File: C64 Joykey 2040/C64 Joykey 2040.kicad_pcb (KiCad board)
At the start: 2 copper layers, 99.7 x 74.9 mm, 62 parts, among them J1 Port_1, J2 Port_2, M1 Mounting, M2 Mounting, M3 Mounting, M4 Mounting, Q1 2N3904, SW1 P2_FIRE1, SW10 P1_FIRE2, SW11 P1_FIRE3, SW12 P1_FIRE4, SW2 P2_FIRE2, SW3 P2_FIRE3, SW4 UP, SW5 DOWN, SW6 LEFT, SW7 RIGHT, SW8 RESET, SW9 P1_FIRE1

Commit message: First layout drafted
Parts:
- removed A1: Arduino_Pro_Micro, arduino_pro_micro:Arduino_Pro_Micro
- removed JP4: DEFAULT_FW, solder_bridge:bridge
- removed JP5: LED_SEL, solder_bridge:select
- removed JP6: DEFAULT_FW, solder_bridge:bridge_r
- removed JP9: ARD_EN, Connector_PinHeader_2.54mm:PinHeader_1x02_P2.54mm_Vertical
- removed R14, R15, R16, R17, R18, R19, R20, R21, R5: 10k, Resistor_THT:R_Axial_DIN0207_L6.3mm_D2.5mm_P10.16mm_Horizontal
- added D12: 1N4148, Diode_THT:D_DO-35_SOD27_P7.62mm_Horizontal, F.Cu at (151.1, 109.9)
- added D13: 1N4148, Diode_THT:D_DO-35_SOD27_P7.62mm_Horizontal, F.Cu at (169.5, 117.5)
- added D14: 1N4148, Diode_THT:D_DO-35_SOD27_P7.62mm_Horizontal, F.Cu at (172.7, 117.5)
- added D15: 1N4148, Diode_THT:D_DO-35_SOD27_P7.62mm_Horizontal, F.Cu at (179.1, 117.5)
- added D16: 1N4148, Diode_THT:D_DO-35_SOD27_P7.62mm_Horizontal, F.Cu at (205.1, 106.0)
- added D17: 1N4148, Diode_THT:D_DO-35_SOD27_P7.62mm_Horizontal, F.Cu at (175.9, 117.5)
- added D18: 1N4148, Diode_THT:D_DO-35_SOD27_P7.62mm_Horizontal, F.Cu at (182.2, 117.5)
- added D19: 1N4148, Diode_THT:D_DO-35_SOD27_P7.62mm_Horizontal, F.Cu at (194.3, 111.8)
- added D20: 1N4148, Diode_THT:D_DO-35_SOD27_P7.62mm_Horizontal, F.Cu at (190.5, 102.2)
- added D21: 1N4148, Diode_THT:D_DO-35_SOD27_P7.62mm_Horizontal, F.Cu at (205.1, 96.5)
- added D22: 1N4148, Diode_THT:D_DO-35_SOD27_P7.62mm_Horizontal, F.Cu at (205.1, 99.7)
- added D23: 1N4148, Diode_THT:D_DO-35_SOD27_P7.62mm_Horizontal, F.Cu at (205.1, 102.9)
- added D24: 1N4148, Diode_THT:D_DO-35_SOD27_P7.62mm_Horizontal, F.Cu at (143.5, 111.8)
- added D25: 1N4148, Diode_THT:D_DO-35_SOD27_P7.62mm_Horizontal, F.Cu at (185.4, 117.5)
- added J3: LED_EN, TestPoint:TestPoint_THTPad_D1.5mm_Drill0.7mm, F.Cu at (217.8, 122.6)
- added J4: Expansion, Connector_PinHeader_2.54mm:PinHeader_1x04_P2.54mm_Vertical, F.Cu at (144.1, 133.3)
- added R23: 10k, Resistor_THT:R_Axial_DIN0207_L6.3mm_D2.5mm_P10.16mm_Horizontal, F.Cu at (217.8, 116.8)
- added SW13: P1_FIRE6, Button_Switch_THT:SW_Tactile_SPST_Angled_PTS645Vx31-2LFS, F.Cu at (206.7, 154.7)
- added U1: RP2040-Zero, pi_pico:RP2040-Zero, F.Cu at (177.2, 108.6)
- D2: value SYS -> POL
- D4: value 1n4148 -> 1N4148
- Q1: footprint 2n3904:2N3904_TO-92_Horizontal_FlatSideDown -> Package_TO_SOT_THT:TO-92_Inline_Wide
- R4: value 330 -> 100
- SW1: value P2_FIRE1 -> UP
- SW11: value P1_FIRE3 -> P2_FIRE3; footprint Button_Switch_THT:SW_Tactile_SPST_Angled_PTS645Vx31-2LFS -> Button_Switch_Keyboard:SW_Cherry_MX_1.00u_PCB
- SW12: value P1_FIRE4 -> P1_FIRE5
- SW2: value P2_FIRE2 -> DOWN
- SW3: value P2_FIRE3 -> LEFT
- SW4: value UP -> RIGHT
- SW5: value DOWN -> P1_FIRE4; footprint Button_Switch_Keyboard:SW_Cherry_MX_1.00u_PCB -> Button_Switch_THT:SW_Tactile_SPST_Angled_PTS645Vx31-2LFS
- SW6: value LEFT -> P2_FIRE1
- SW7: value RIGHT -> P1_FIRE1; footprint Button_Switch_Keyboard:SW_Cherry_MX_1.00u_PCB -> Button_Switch_THT:SW_Tactile_SPST_Angled_PTS645Vx31-2LFS
- SW8: value RESET -> P1_FIRE3; footprint Button_Switch_THT:SW_PUSH_6mm -> Button_Switch_THT:SW_Tactile_SPST_Angled_PTS645Vx31-2LFS
- SW9: value P1_FIRE1 -> P2_FIRE2; footprint Button_Switch_THT:SW_Tactile_SPST_Angled_PTS645Vx31-2LFS -> Button_Switch_Keyboard:SW_Cherry_MX_1.00u_PCB
- moved SW7 67.4 mm to (155.4, 154.7)
- moved SW11 56.5 mm to (154.3, 104.1)
- moved SW1 51.5 mm to (201.3, 125.1)
- moved SW2 51.5 mm to (201.3, 146.1)
- moved SW3 49.3 mm to (180.3, 146.1)
- moved G*** 48.7 mm to (177.5, 124.0)
- moved D4 34.1 mm to (147.3, 104.1), turned to -90 degrees
- moved R13 32.1 mm to (228.0, 127.6)
- moved SW8 31.6 mm to (179.4, 154.7), turned to 180 degrees
- moved SW5 30.7 mm to (230.7, 154.7)
- moved SW4 29.6 mm to (222.2, 146.1)
- moved SW9 29.6 mm to (154.3, 125.1)
- moved R1 28.4 mm to (217.8, 113.0)
- moved SW6 26.0 mm to (154.3, 146.1)
- moved R2 25.9 mm to (217.8, 109.2)
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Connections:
- D4 pad 1: /FIRE1_OUT -> Net-(D12-K)
- D4 pad 2: Net-(D4-A) -> FIRE3_POL
- R13 pad 2: /UNDERGLOW -> Net-(J3-Pin_1)
- R3 pad 2: Net-(JP5-C) -> VCC
- R4 pad 2: /SYS -> Net-(D12-K)
- SW1 pad 1: Net-(JP4-Pad1) -> P2_UP
- SW10 pad 2: FIRE2_POL -> GND
- SW11 pad 1: P1_FIRE3 -> Net-(JP3-C)
- SW12 pad 1: P1_FIRE4 -> P1_FIRE5
- SW2 pad 1: Net-(JP6-Pad1) -> P2_DOWN
- SW2 pad 2: FIRE2_POL -> GND
- SW3 pad 1: Net-(JP3-C) -> P2_LEFT
- SW3 pad 2: FIRE3_POL -> GND
- SW4 pad 1: P2_UP -> P2_RIGHT
- SW5 pad 1: P2_DOWN -> P1_FIRE4
- SW6 pad 1: P2_LEFT -> P2_FIRE1
- SW7 pad 1: P2_RIGHT -> P1_FIRE1
- SW8 pad 1: Net-(A1-RST) -> P1_FIRE3
- SW9 pad 1: P1_FIRE1 -> P2_FIRE2
- SW9 pad 2: GND -> FIRE2_POL
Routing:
- net Net-(A1-D18): track 78.1 -> 0.00 mm
- net P1_FIRE5: track 0.00 -> 78.0 mm, vias 0 -> 3
- net P1_FIRE2: track 174.7 -> 100.8 mm, vias 2 -> 3
- net I2C_SDA: track 0.00 -> 73.6 mm
- net I2C_SCL: track 0.00 -> 68.3 mm
- net +3V3: track 0.00 -> 65.1 mm
- net /B2: track 0.00 -> 62.9 mm, vias 0 -> 2
- net P1_FIRE6: track 0.00 -> 51.7 mm, vias 0 -> 2
- net /FIRE1_IN: track 51.5 -> 0.00 mm, vias 2 -> 0
- net Net-(A1-D14): track 51.1 -> 0.00 mm, vias 2 -> 0
- net FIRE3_POL: track 142.6 -> 91.7 mm, vias 4 -> 2
- net Net-(A1-RST): track 49.2 -> 0.00 mm, vias 2 -> 0
- net /SYS: track 49.2 -> 0.00 mm, vias 1 -> 0
- net Net-(JP4-Pad1): track 48.3 -> 0.00 mm
- net Net-(A1-D19): track 46.0 -> 0.00 mm, vias 2 -> 0
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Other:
- board text added: "(A1)"
- board text added: "(B1)"
- board text added: "(B2)"
- board text added: "(B3)"
- board text added: "(B4)"
- board text added: "(R1)"
- board text added: "(R2)"
- board text added: "(S1)"
- board text added: "(S2)"
- board text added: "2040 Revision A github.com/tebl"
- board text added: "IMPORTANT! Always configure FIRE2/FIRE3 polarity according to what's required by the system. Leave unjumpered (N/C) if you are not sure. You break it, you fix it!"
- board text added: "P1 F5"
- board text added: "P1 F6"
- board text removed: "1-2 Always ON 2-3 Arduino"
- board text removed: "ARD_EN"
- board text removed: "Default FW"
- board text removed: "IMPORTANT! Configure FIRE2/FIRE3 polarity according to what is required by the system, leave unjumpered (N/C) if you are not sure. You break it, you fix it!"
- board text removed: "Install Arduino Pro Micro, if needed for USB function. Hold down LEFT + RIGHT key on powerup to enable. FIRE2/3 polarity must be set to GND, keys will be disabled in USB-mode if not."
- board text removed: "PCB Revision F github.com/tebl"

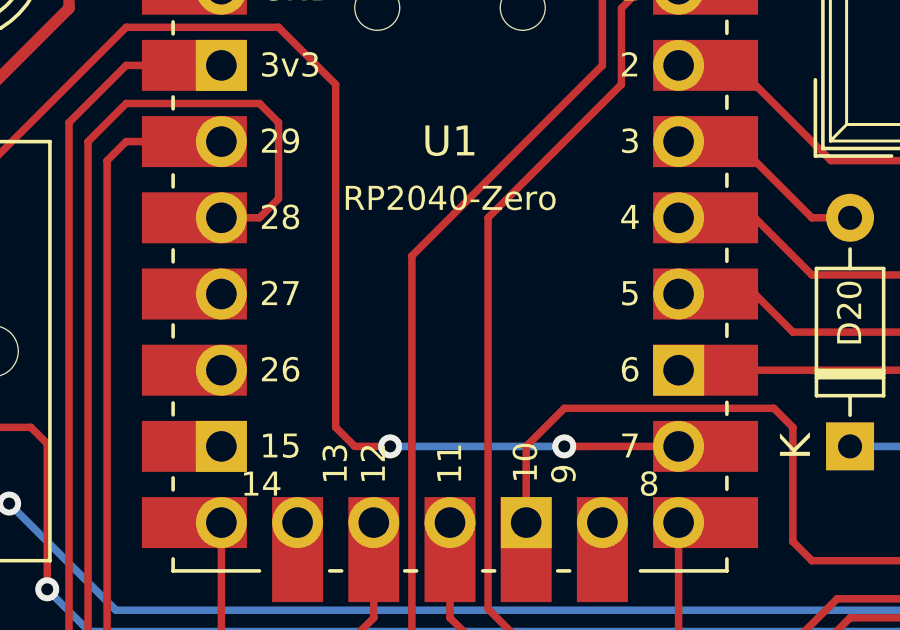
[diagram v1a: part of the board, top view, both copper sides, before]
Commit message: Arcade 2040, and some cleanup
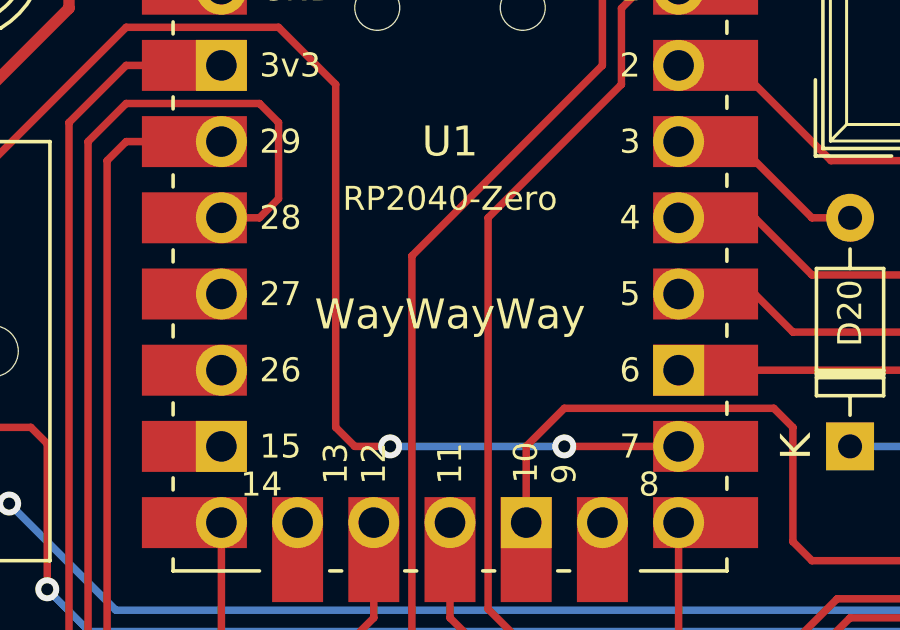
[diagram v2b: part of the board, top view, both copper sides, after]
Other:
- board text added: "WayWayWay"
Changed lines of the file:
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@@
 		(tags "tactile switch SPST angled PTS645VL31-2 LFS C&K Button")
 		(property "Reference" "SW8"
-			(at 2.25 1.68 360)
+			(at 2.25 1.68 0)
 			(layer "F.SilkS")
 			(effects
@@
 		)
 		(property "Value" "P1_FIRE3"
-			(at 2.25 5.38988 360)
+			(at 2.25 5.38988 0)
 			(layer "F.Fab")
 			(effects
@@
 		)
 		(fp_text user "${REFERENCE}"
-			(at 2.25 1.68 360)
+			(at 2.25 1.68 0)
 			(layer "F.Fab")
 			(effects
@@
 		(tags "to-92 sc-43 sc-43a sot54 PA33 transistor")
 		(property "Reference" "Q1"
-			(at -0.635 1.905 360)
+			(at -0.635 1.905 0)
 			(layer "F.SilkS")
 			(effects
@@
 		)
 		(property "Value" "2N3904"
-			(at 2.54 2.79 360)
+			(at 2.54 2.79 0)
 			(layer "F.Fab")
 			(effects
@@
 		)
 		(fp_text user "${REFERENCE}"
-			(at 2.54 0 360)
+			(at 2.54 0 0)
 			(layer "F.Fab")
 			(effects
@@
 		(tags "Diode DO-35_SOD27 series Axial Horizontal pin pitch 7.62mm  length 4mm diameter 2mm")
 		(property "Reference" "D16"
-			(at 4.445 0 360)
+			(at 4.445 0 0)
 			(layer "F.SilkS")
 			(effects
@@
 		)
 		(property "Value" "1N4148"
-			(at 3.81 2.12 360)
+			(at 3.81 2.12 0)
 			(layer "F.Fab")
 			(effects
@@
 		)
 		(fp_text user "K"
-			(at 0 -1.8 360)
+			(at 0 -1.8 0)
 			(layer "F.SilkS")
 			(effects
@@
 		)
 		(fp_text user "K"
-			(at 0 -1.8 360)
+			(at 0 -1.8 0)
 			(layer "F.Fab")
 			(effects
@@
 		)
 		(fp_text user "${REFERENCE}"
-			(at 4.11 0 360)
+			(at 4.11 0 0)
 			(layer "F.Fab")
 			(effects
@@
 		(tags "Diode DO-35_SOD27 series Axial Horizontal pin pitch 7.62mm  length 4mm diameter 2mm")
 		(property "Reference" "D23"
-			(at 4.445 0 360)
+			(at 4.445 0 0)
 			(layer "F.SilkS")
 			(effects
@@
 		)
 		(property "Value" "1N4148"
-			(at 3.81 2.12 360)
+			(at 3.81 2.12 0)
 			(layer "F.Fab")
 			(effects
@@
 		)
 		(fp_text user "K"
-			(at 0 -1.8 360)
+			(at 0 -1.8 0)
 			(layer "F.SilkS")
 			(effects
@@
 		)
 		(fp_text user "${REFERENCE}"
-			(at 4.11 0 360)
+			(at 4.11 0 0)
 			(layer "F.Fab")
 			(effects
@@
 		)
 		(fp_text user "K"
-			(at 0 -1.8 360)
+			(at 0 -1.8 0)
 			(layer "F.Fab")
 			(effects
@@
 		(tags "tactile switch SPST angled PTS645VL31-2 LFS C&K Button")
 		(property "Reference" "SW13"
-			(at 2.25 1.68 360)
+			(at 2.25 1.68 0)
 			(layer "F.SilkS")
 			(effects
@@
 		)
 		(property "Value" "P1_FIRE6"
-			(at 2.25 5.38988 360)
+			(at 2.25 5.38988 0)
 			(layer "F.Fab")
 			(effects
@@
 		)
 		(fp_text user "${REFERENCE}"
-			(at 2.25 1.68 360)
+			(at 2.25 1.68 0)
 			(layer "F.Fab")
 			(effects
@@
 		)
 		(property "Footprint" "Button_Switch_Keyboard:SW_Cherry_MX_1.00u_PCB"
-			(at 0 0 360)
+			(at 0 0 0)
 			(layer "F.Fab")
 			(hide yes)
@@
 		)
 		(property "Datasheet" ""
-			(at 0 0 360)
+			(at 0 0 0)
 			(layer "F.Fab")
 			(hide yes)
@@
 		)
 		(property "Description" ""
-			(at 0 0 360)
+			(at 0 0 0)
 			(layer "F.Fab")
 			(hide yes)
@@
 		)
 		(fp_text user "${REFERENCE}"
-			(at -2.54 -2.794 360)
+			(at -2.54 -2.794 0)
 			(layer "F.Fab")
 			(effects
@@
 		(tags "Diode DO-35_SOD27 series Axial Horizontal pin pitch 7.62mm  length 4mm diameter 2mm")
 		(property "Reference" "D21"
-			(at 4.445 0 360)
+			(at 4.445 0 0)
 			(layer "F.SilkS")
 			(effects
@@
 		)
 		(property "Value" "1N4148"
-			(at 3.81 2.12 360)
+			(at 3.81 2.12 0)
 			(layer "F.Fab")
 			(effects
@@
 		)
 		(fp_text user "K"
-			(at 0 -1.8 360)
+			(at 0 -1.8 0)
 			(layer "F.SilkS")
 			(effects
@@
 		)
 		(fp_text user "K"
-			(at 0 -1.8 360)
+			(at 0 -1.8 0)
 			(layer "F.Fab")
 			(effects
@@
 		)
 		(fp_text user "${REFERENCE}"
-			(at 4.11 0 360)
+			(at 4.11 0 0)
 			(layer "F.Fab")
 			(effects
@@
 		)
 		(property "Value" "10k"
-			(at 6.35 0 360)
+			(at 6.35 0 0)
 			(layer "F.SilkS")
 			(effects
@@
 		)
 		(fp_text user "${REFERENCE}"
-			(at 5.08 0 360)
+			(at 5.08 0 0)
 			(layer "F.Fab")
 			(effects
@@
 		(tags "Through hole pin header THT 1x04 2.54mm single row")
 		(property "Reference" "J4"
-			(at 0 -2.54 360)
+			(at 0 -2.54 0)
 			(layer "F.SilkS")
 			(effects
@@
 		(tags "Diode DO-35_SOD27 series Axial Horizontal pin pitch 7.62mm  length 4mm diameter 2mm")
 		(property "Reference" "D22"
-			(at 4.445 0 360)
+			(at 4.445 0 0)
 			(layer "F.SilkS")
 			(effects
@@
 		)
 		(property "Value" "1N4148"
-			(at 3.81 2.12 360)
+			(at 3.81 2.12 0)
 			(layer "F.Fab")
 			(effects
@@
 		)
 		(fp_text user "K"
-			(at 0 -1.8 360)
+			(at 0 -1.8 0)
 			(layer "F.SilkS")
 			(effects
@@
 		)
 		(fp_text user "${REFERENCE}"
-			(at 4.11 0 360)
+			(at 4.11 0 0)
 			(layer "F.Fab")
 			(effects
@@
 		)
 		(fp_text user "K"
-			(at 0 -1.8 360)
+			(at 0 -1.8 0)
 			(layer "F.Fab")
 			(effects
@@
 		)
 		(property "Footprint" "Button_Switch_Keyboard:SW_Cherry_MX_1.00u_PCB"
-			(at 0 0 360)
+			(at 0 0 0)
 			(layer "F.Fab")
 			(hide yes)
@@
 		)
 		(property "Datasheet" ""
-			(at 0 0 360)
+			(at 0 0 0)
 			(layer "F.Fab")
 			(hide yes)
@@
 		)
 		(property "Description" ""
-			(at 0 0 360)
+			(at 0 0 0)
 			(layer "F.Fab")
 			(hide yes)
@@
 		)
 		(fp_text user "${REFERENCE}"
-			(at -2.54 -2.794 360)
+			(at -2.54 -2.794 0)
 			(layer "F.Fab")
 			(effects
@@
 		)
 	)
+	(gr_text "WayWayWay"
+		(at 177.165 98.425 0)
+		(layer "F.SilkS")
+		(effects
+			(font
+				(size 1 1)
+				(thickness 0.1)
+			)
+			(justify bottom)
+		)
+	)

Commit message: Add diode for power from USB
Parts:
- added D26: 1n5819, Diode_THT:D_DO-41_SOD81_P10.16mm_Horizontal, F.Cu at (149.9, 130.5)
- moved D12 1.91 mm to (153.0, 109.9)
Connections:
- D25 pad 2: /R2 -> /L1
- U1 pad 1: VCC -> Net-(D26-A)
- U1 pad 15: /R2 -> /R2_1
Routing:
- net Net-(D26-A): track 0.00 -> 52.3 mm, vias 0 -> 1
- net VCC: track 410.9 -> 385.2 mm
- net /L1: track 0.00 -> 20.3 mm, vias 0 -> 1
- net Net-(D5-K): track 48.0 -> 41.5 mm
- net /R2: track 5.34 -> 0.00 mm
- net FIRE2_POL: track 84.4 -> 81.0 mm
- net Net-(D12-K): track 10.5 -> 12.4 mm
- net +3V3: track 65.1 -> 66.5 mm
- net FIRE3_POL: track 91.7 -> 90.3 mm
- net P2_FIRE2: track 125.5 -> 126.9 mm
- net /B2: track 62.9 -> 61.9 mm
- net I2C_SCL: track 68.3 -> 67.6 mm
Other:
- board text added: "(L1)"
- board text added: "2040 Revision B github.com/tebl"
- board text removed: "(R2)"
- board text removed: "2040 Revision A github.com/tebl"

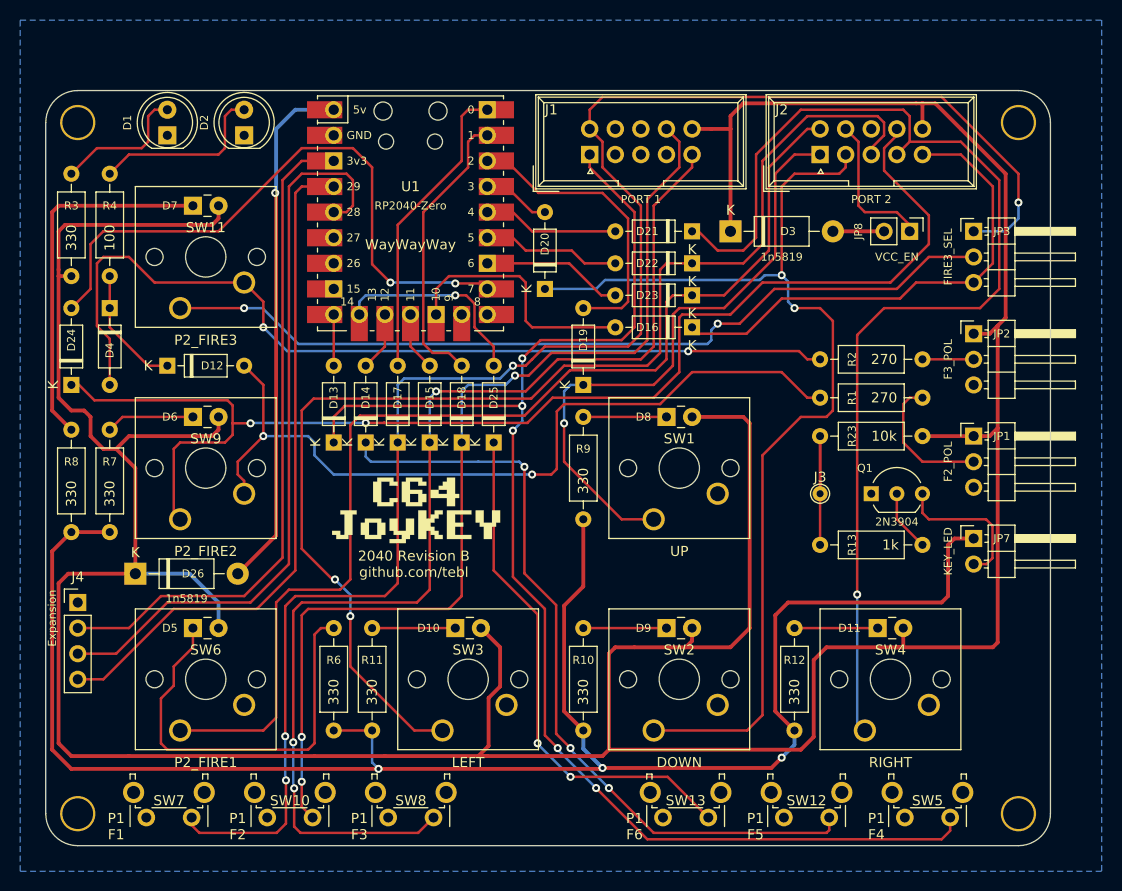
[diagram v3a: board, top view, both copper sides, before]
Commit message: Try adding underglow to GPIO15
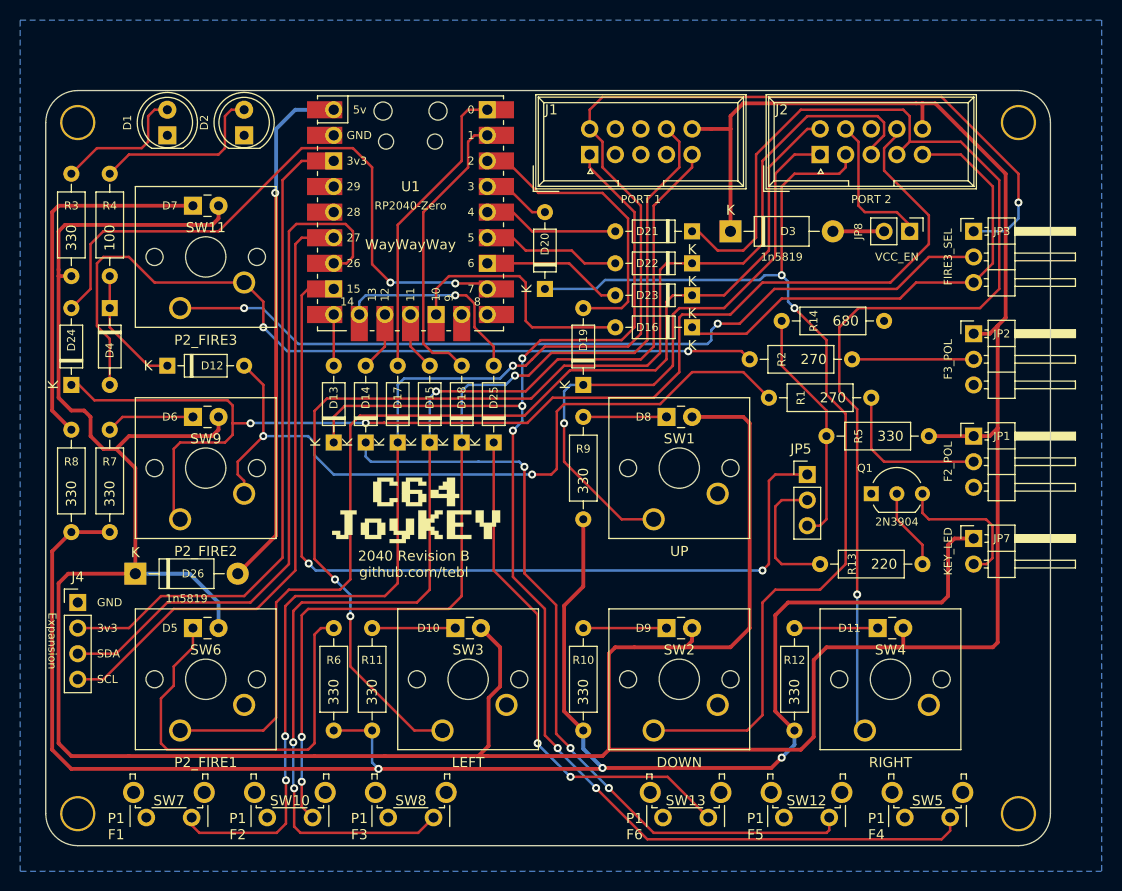
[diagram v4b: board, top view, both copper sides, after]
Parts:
- removed J3: LED_EN, TestPoint:TestPoint_THTPad_D1.5mm_Drill0.7mm
- removed R23: 10k, Resistor_THT:R_Axial_DIN0207_L6.3mm_D2.5mm_P10.16mm_Horizontal
- added JP5: LED_PIN, Connector_PinHeader_2.54mm:PinHeader_1x03_P2.54mm_Vertical, F.Cu at (216.5, 120.7)
- added R14: 680, Resistor_THT:R_Axial_DIN0207_L6.3mm_D2.5mm_P10.16mm_Horizontal, F.Cu at (224.2, 105.4)
- added R5: 330, Resistor_THT:R_Axial_DIN0207_L6.3mm_D2.5mm_P10.16mm_Horizontal, F.Cu at (218.4, 116.8)
- R13: value 1k -> 220
- moved R2 6.99 mm to (210.8, 109.2)
- moved R1 5.08 mm to (212.7, 113.0)
- moved R13 1.90 mm to (228.0, 129.5)
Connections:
- U1 pad 4: I2C_SCL -> unconnected-(U1-GPIO29_ADC3-Pad4)_1
- U1 pad 5: I2C_SDA -> unconnected-(U1-GPIO28_ADC2-Pad5)
- U1 pad 6: /R3_1 -> I2C_SCL
- U1 pad 7: /L3_1 -> I2C_SDA
- U1 pad 8: /A2 -> LED_EN
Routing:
- net LED_EN: track 0.00 -> 88.9 mm, vias 0 -> 2
- net Net-(JP5-B): track 0.00 -> 23.7 mm
- net Net-(JP2-C): track 5.08 -> 12.1 mm
- net FIRE3_POL: track 90.3 -> 83.3 mm
- net I2C_SCL: track 67.6 -> 62.5 mm
- net FIRE2_POL: track 81.0 -> 75.9 mm
- net I2C_SDA: track 73.9 -> 69.3 mm
- net Net-(JP5-C): track 16.5 -> 13.2 mm
- net P2_RIGHT: track 114.4 -> 117.4 mm
- net Net-(JP1-C): track 13.8 -> 15.8 mm
- net P2_LEFT: track 122.8 -> 120.9 mm
- net Net-(Q1-B): track 6.13 -> 8.04 mm
- net P2_DOWN: track 104.3 -> 105.0 mm
- net VCC: track 385.2 -> 384.5 mm
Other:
- board text added: "(GPIO15)"
- board text added: "3v3"
- board text added: "LED_PIN"
- board text added: "SCL"
- board text added: "SDA"
